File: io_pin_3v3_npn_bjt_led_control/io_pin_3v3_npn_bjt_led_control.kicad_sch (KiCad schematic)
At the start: 6 parts, among them Q1 NPN

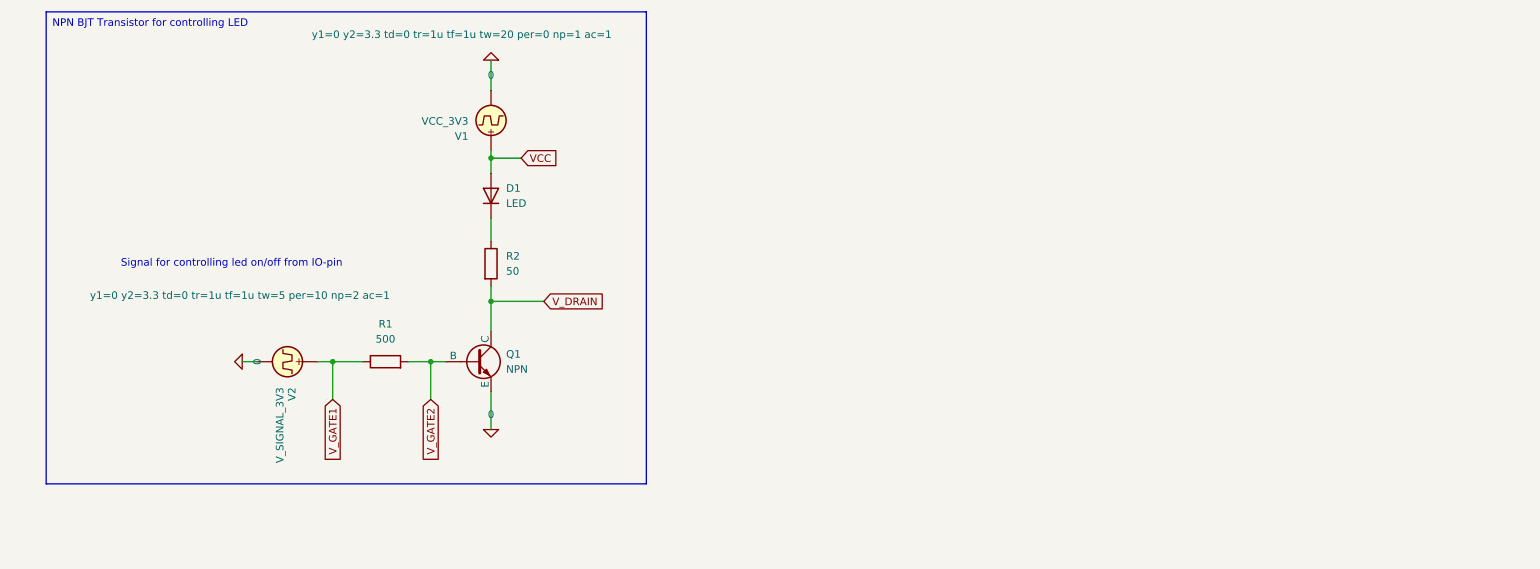
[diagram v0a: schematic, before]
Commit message: added comments to 3v3 npn bjt example
Signed-off-by: Mika Laitio <lamikr@gmail.com>
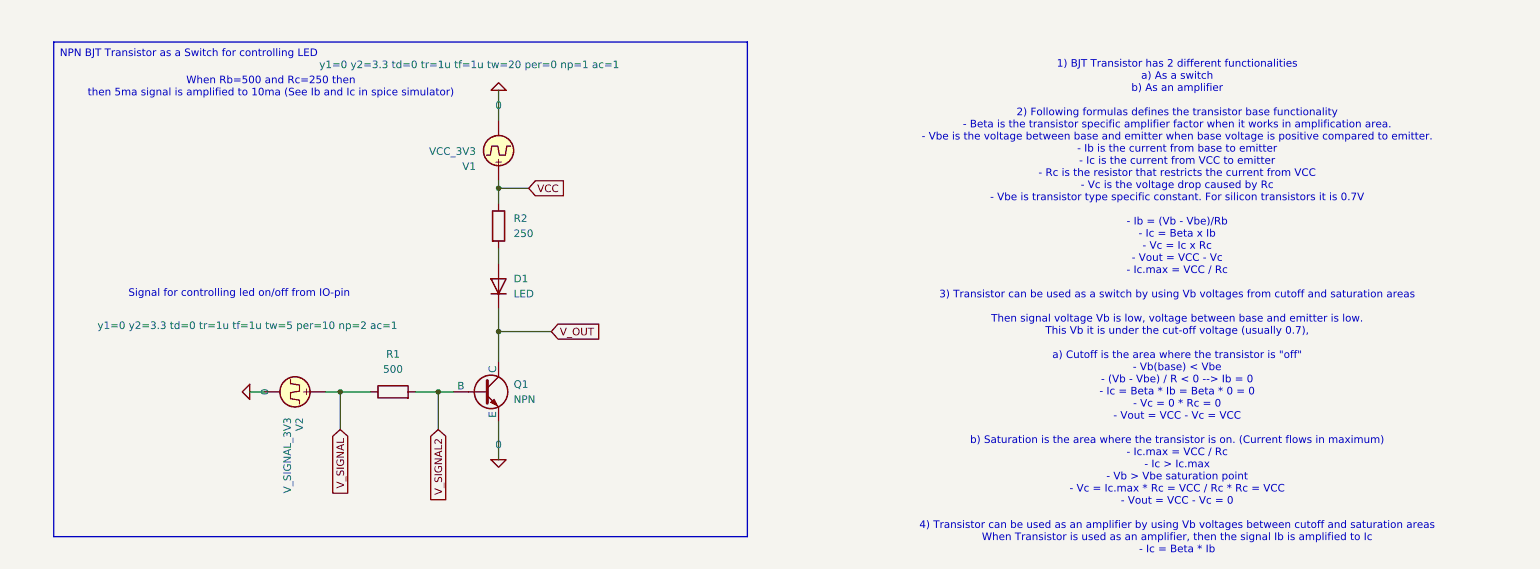
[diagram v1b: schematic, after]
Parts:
- R2: value 50 -> 250
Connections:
- net VCC: now also R2.1; no longer D1.2 (A)
- net V_OUT: now reaches D1.1 (K)
- net V_OUT: now also Q1.1 (C); no longer R2.1
- net V_DRAIN: no longer names the net of R2.2
- net V_DRAIN: now also D1.2 (A); no longer Q1.1 (C)
- net V_GATE1 renamed V_SIGNAL
- net V_GATE2 renamed V_SIGNAL2
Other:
- note added: "1) BJT Transistor has 2 different functionalities a) As a switch b) As an amplifier 2) Following formulas defines the transistor base functionality - Beta is the transistor specific amplifier factor when it works in amplification area. - Vbe is the voltage between base and emitter when base voltage is positive compared to emitter. - Ib is the current from base to emitter - Ic is the current from 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"
- note added: "When Rb=500 and Rc=250 then then 5ma signal is amplified to 10ma (See Ib and Ic in spice simulator)"
- moved on the sheet: D1, Q1, R1, R2, V1, V2
